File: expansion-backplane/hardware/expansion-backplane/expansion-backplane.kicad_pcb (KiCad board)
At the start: 2 copper layers, 119 x 51 mm, 26 parts, among them J1 Barrel_Jack, SW1 SW_SPDT, U1 74AHCT126

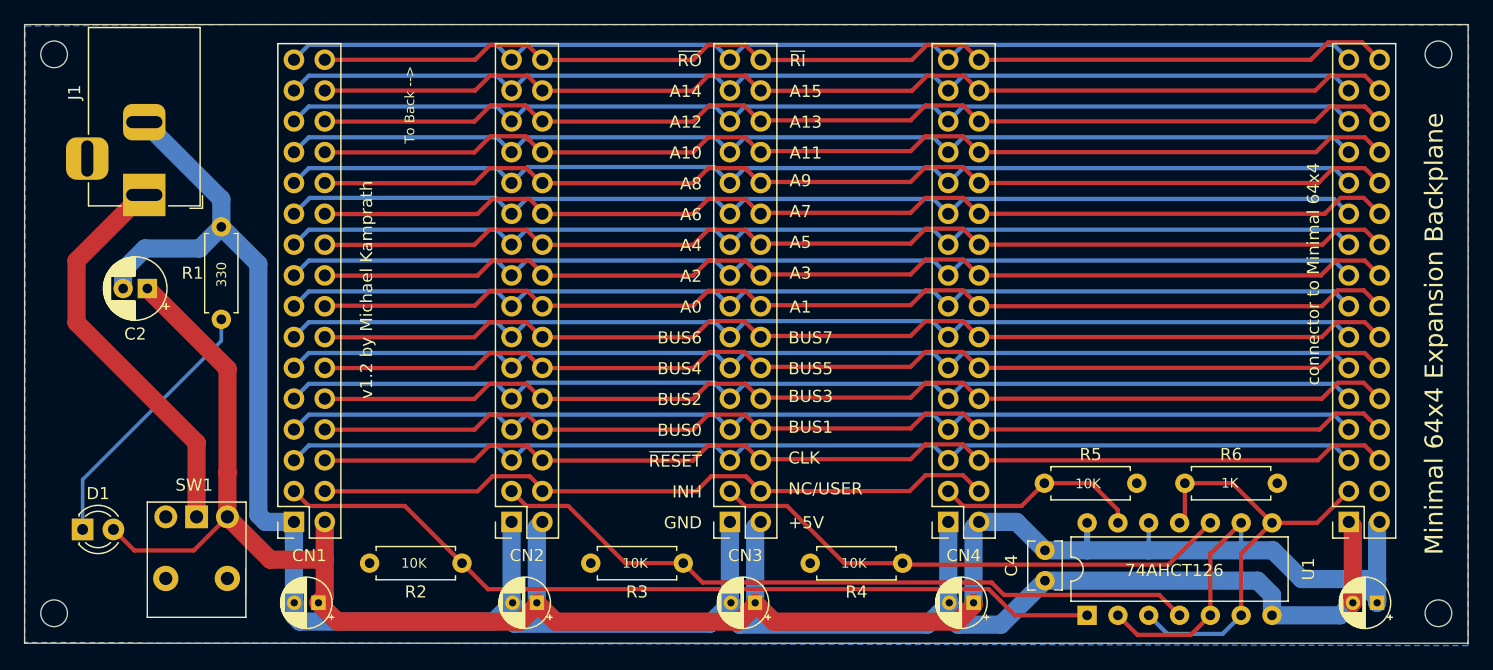
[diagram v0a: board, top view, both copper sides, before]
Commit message: Hardware Multiplier (#1)
Created a hardware multiplier for the Minimal 64x4
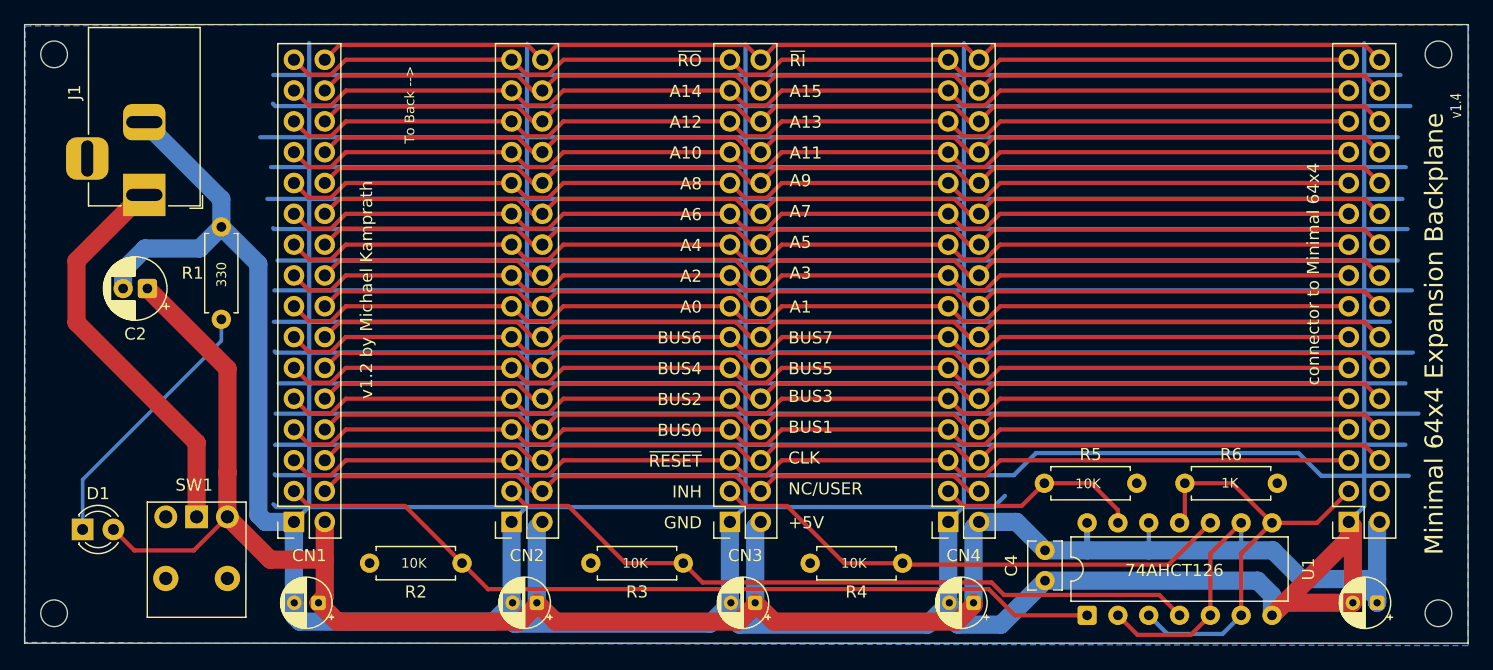
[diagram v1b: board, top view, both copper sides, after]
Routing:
- net GND: track 185.5 -> 1765.1 mm
- net A11: track 91.6 -> 91.0 mm
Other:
- board text added: "v1.4"
